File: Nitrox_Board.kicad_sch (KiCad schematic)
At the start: 9 parts

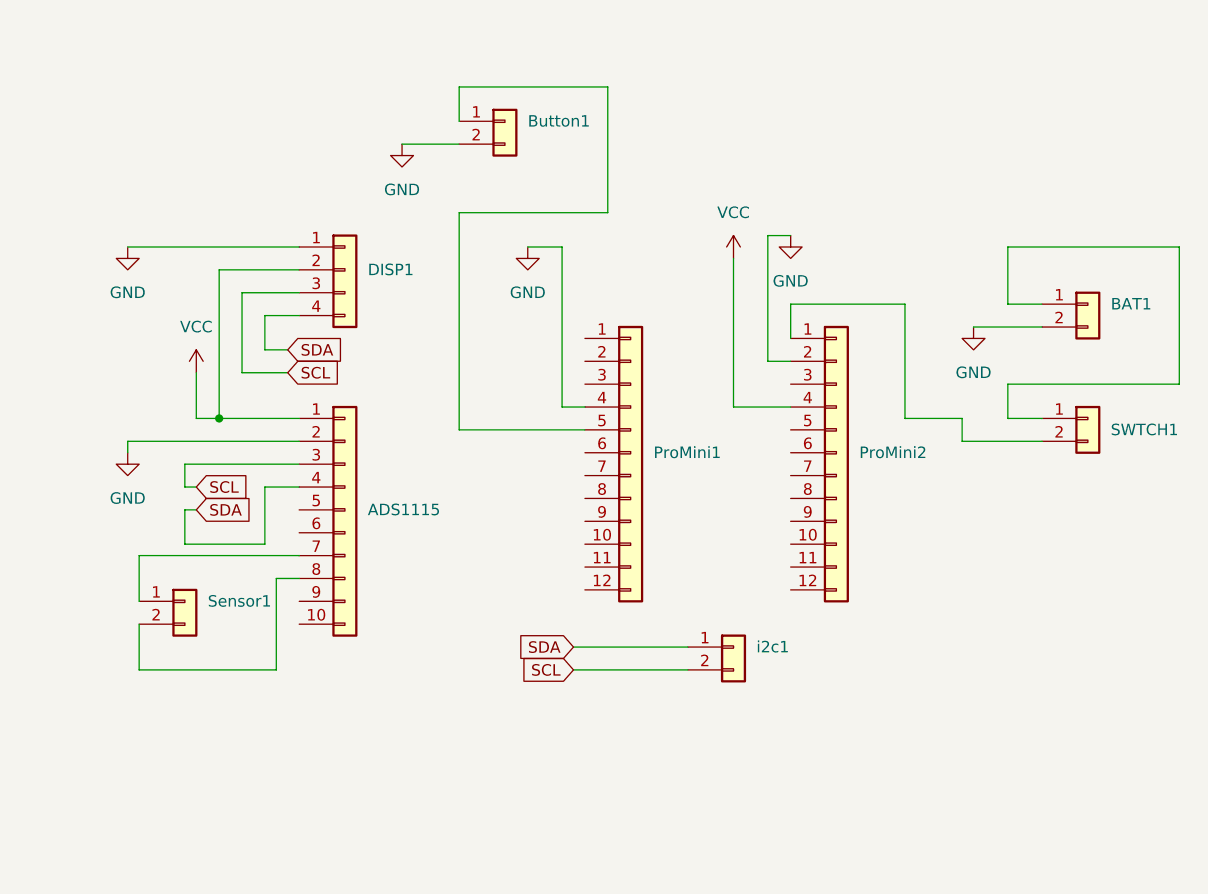
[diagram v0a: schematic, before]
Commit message: Initial Sketch
Pending some breadboard work, basic diagram and pinouts.
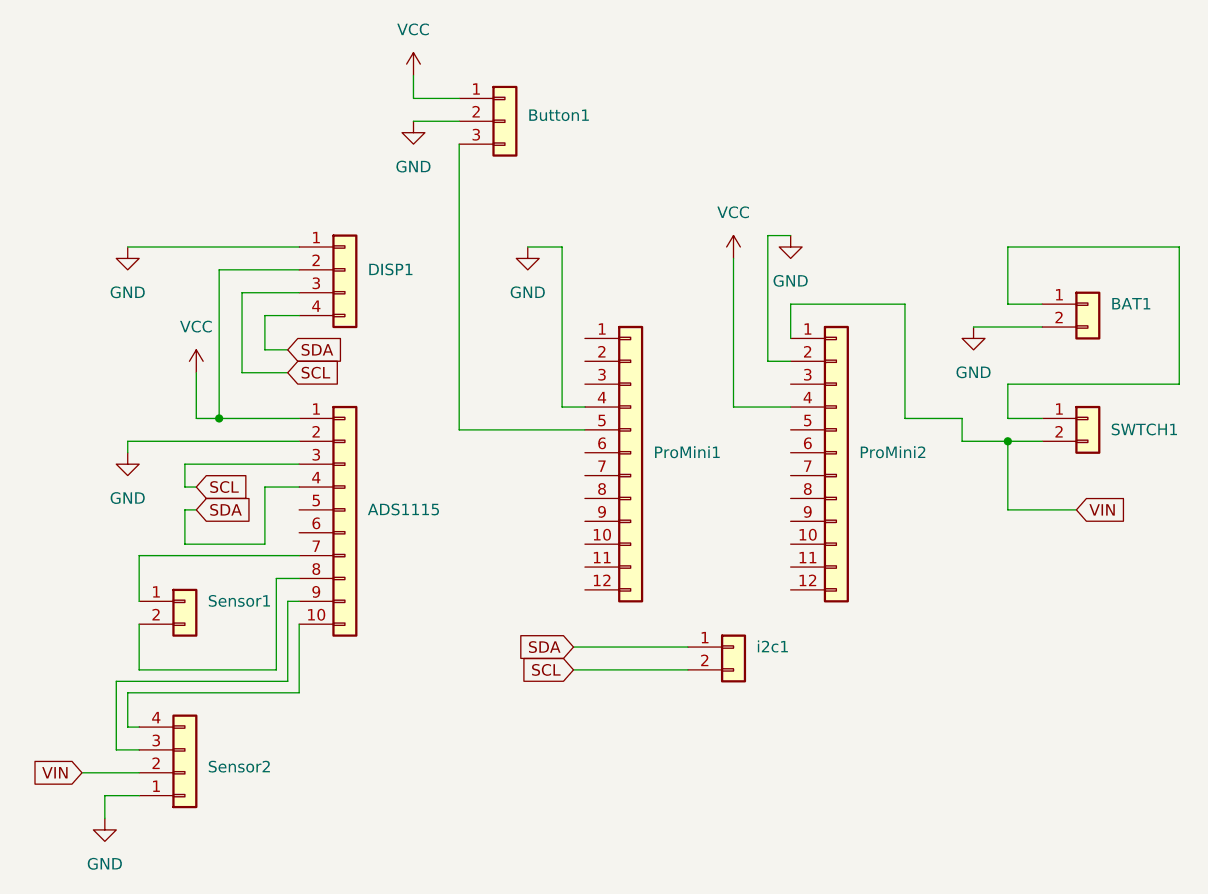
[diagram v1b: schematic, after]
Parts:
- added Sensor2: ~, Connector_JST:JST_XH_B2B-XH-A_1x02_P2.50mm_Vertical, symbol Connector_Generic:Conn_01x04
- Button1: symbol Connector_Generic:Conn_01x02 -> Connector_Generic:Conn_01x03
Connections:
- net GND: now also Sensor2.1 (Pin_1)
- net VCC: now also Button1.1 (Pin_1)
- net VIN: now reaches ProMini2.1 (Pin_1), SWTCH1.2 (Pin_2)
- net VIN: now also Sensor2.2 (Pin_2)
- net at ProMini1.5 (Pin_5): now also Button1.3 (Pin_3); no longer Button1.1 (Pin_1)
- net at ADS1115.10 (Pin_10): now also Sensor2.4 (Pin_4)
- net at ADS1115.9 (Pin_9): now also Sensor2.3 (Pin_3)

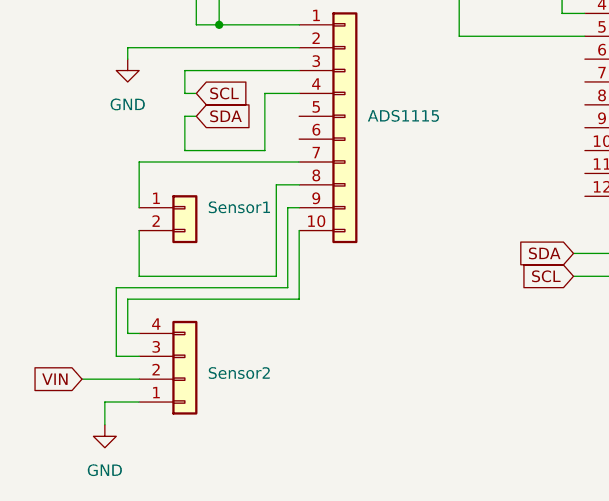
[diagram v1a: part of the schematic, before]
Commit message: CO Sensor Changes
Add CO Sensor Alarm to display render, add CO Sensor to ADC pin 3 (non-diff reading), Add various math/variables for CO Sensor and to differentiate from O2 Sensor, Always calibrate on Boot/Reset, and FREEDOM UNITS (MOD in Feet instead of meters).

PCB Updated to add CO Sensor leads and LED lead for button illumination when on.
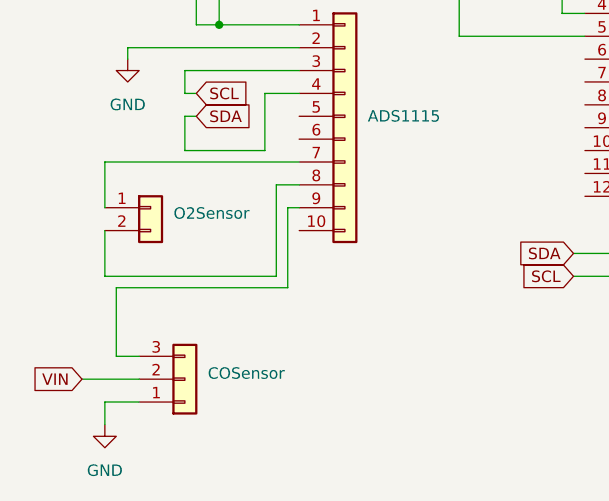
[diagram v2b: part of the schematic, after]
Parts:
- COSensor: renamed from Sensor2; symbol Connector_Generic:Conn_01x04 -> Connector_Generic:Conn_01x03
- renumbered Sensor1 to O2Sensor
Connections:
- net at ADS1115.10 (Pin_10): no longer COSensor.4 (Pin_4)
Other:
- moved on the sheet: O2Sensor
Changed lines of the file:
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@@
 	(wire
 		(pts
-			(xy 26.67 86.36) (xy 41.91 86.36)
-		)
-		(stroke
-			(width 0)
-			(type default)
-		)
-	)
-	(wire
-		(pts
-			(xy 26.67 73.66) (xy 44.45 73.66)
+			(xy 22.86 86.36) (xy 41.91 86.36)
+		)
+		(stroke
+			(width 0)
+			(type default)
+		)
+	)
+	(wire
+		(pts
+			(xy 22.86 73.66) (xy 44.45 73.66)
 		)
 		(stroke
@@
 	(wire
 		(pts
+			(xy 123.19 68.58) (xy 130.81 68.58)
+		)
+		(stroke
+			(width 0)
+			(type default)
+		)
+	)
+	(wire
+		(pts
+			(xy 40.64 72.39) (xy 31.75 72.39)
+		)
+		(stroke
+			(width 0)
+			(type default)
+		)
+	)
+	(wire
+		(pts
+			(xy 74.93 83.82) (xy 87.63 83.82)
+		)
+		(stroke
+			(width 0)
+			(type default)
+		)
+	)
+	(wire
+		(pts
+			(xy 119.38 48.26) (xy 127 48.26)
+		)
+		(stroke
+			(width 0)
+			(type default)
+		)
+	)
+	(wire
+		(pts
+			(xy 40.64 46.99) (xy 40.64 50.8)
+		)
+		(stroke
+			(width 0)
+			(type default)
+		)
+	)
+	(wire
+		(pts
+			(xy 92.71 57.15) (xy 99.06 57.15)
+		)
+		(stroke
+			(width 0)
+			(type default)
+		)
+	)
+	(wire
+		(pts
+			(xy 41.91 76.2) (xy 44.45 76.2)
+		)
+		(stroke
+			(width 0)
+			(type default)
+		)
+	)
+	(wire
+		(pts
+			(xy 22.86 81.28) (xy 22.86 86.36)
+		)
+		(stroke
+			(width 0)
+			(type default)
+		)
+	)
+	(wire
+		(pts
+			(xy 57.15 20.32) (xy 57.15 22.86)
+		)
+		(stroke
+			(width 0)
+			(type default)
+		)
+	)
+	(wire
+		(pts
+			(xy 123.19 60.96) (xy 123.19 68.58)
+		)
+		(stroke
+			(width 0)
+			(type default)
+		)
+	)
+	(wire
+		(pts
+			(xy 123.19 45.72) (xy 123.19 39.37)
+		)
+		(stroke
+			(width 0)
+			(type default)
+		)
+	)
+	(wire
+		(pts
+			(xy 127 45.72) (xy 123.19 45.72)
+		)
+		(stroke
+			(width 0)
+			(type default)
+		)
+	)
+	(wire
+		(pts
+			(xy 96.52 52.07) (xy 96.52 38.1)
+		)
+		(stroke
+			(width 0)
+			(type default)
+		)
+	)
+	(wire
+		(pts
+			(xy 38.1 53.34) (xy 43.18 53.34)
+		)
+		(stroke
+			(width 0)
+			(type default)
+		)
+	)
+	(wire
+		(pts
+			(xy 92.71 40.64) (xy 92.71 57.15)
+		)
+		(stroke
+			(width 0)
+			(type default)
+		)
+	)
+	(wire
+		(pts
+			(xy 123.19 54.61) (xy 123.19 58.42)
+		)
+		(stroke
+			(width 0)
+			(type default)
+		)
+	)
+	(wire
+		(pts
 			(xy 24.13 87.63) (xy 43.18 87.63)
 		)
@@
 	(wire
 		(pts
-			(xy 123.19 68.58) (xy 130.81 68.58)
-		)
-		(stroke
-			(width 0)
-			(type default)
-		)
-	)
-	(wire
-		(pts
-			(xy 40.64 72.39) (xy 31.75 72.39)
-		)
-		(stroke
-			(width 0)
-			(type default)
-		)
-	)
-	(wire
-		(pts
-			(xy 74.93 83.82) (xy 87.63 83.82)
-		)
-		(stroke
-			(width 0)
-			(type default)
-		)
-	)
-	(wire
-		(pts
-			(xy 25.4 88.9) (xy 25.4 92.71)
-		)
-		(stroke
-			(width 0)
-			(type default)
-		)
-	)
-	(wire
-		(pts
-			(xy 119.38 48.26) (xy 127 48.26)
-		)
-		(stroke
-			(width 0)
-			(type default)
-		)
-	)
-	(wire
-		(pts
-			(xy 25.4 88.9) (xy 44.45 88.9)
-		)
-		(stroke
-			(width 0)
-			(type default)
-		)
-	)
-	(wire
-		(pts
-			(xy 40.64 46.99) (xy 40.64 50.8)
-		)
-		(stroke
-			(width 0)
-			(type default)
-		)
-	)
-	(wire
-		(pts
-			(xy 92.71 57.15) (xy 99.06 57.15)
-		)
-		(stroke
-			(width 0)
-			(type default)
-		)
-	)
-	(wire
-		(pts
-			(xy 41.91 76.2) (xy 44.45 76.2)
-		)
-		(stroke
-			(width 0)
-			(type default)
-		)
-	)
-	(wire
-		(pts
-			(xy 26.67 81.28) (xy 26.67 86.36)
-		)
-		(stroke
-			(width 0)
-			(type default)
-		)
-	)
-	(wire
-		(pts
-			(xy 57.15 20.32) (xy 57.15 22.86)
-		)
-		(stroke
-			(width 0)
-			(type default)
-		)
-	)
-	(wire
-		(pts
-			(xy 123.19 60.96) (xy 123.19 68.58)
-		)
-		(stroke
-			(width 0)
-			(type default)
-		)
-	)
-	(wire
-		(pts
-			(xy 123.19 45.72) (xy 123.19 39.37)
-		)
-		(stroke
-			(width 0)
-			(type default)
-		)
-	)
-	(wire
-		(pts
-			(xy 127 45.72) (xy 123.19 45.72)
-		)
-		(stroke
-			(width 0)
-			(type default)
-		)
-	)
-	(wire
-		(pts
-			(xy 96.52 52.07) (xy 96.52 38.1)
-		)
-		(stroke
-			(width 0)
-			(type default)
-		)
-	)
-	(wire
-		(pts
-			(xy 38.1 53.34) (xy 43.18 53.34)
-		)
-		(stroke
-			(width 0)
-			(type default)
-		)
-	)
-	(wire
-		(pts
-			(xy 92.71 40.64) (xy 92.71 57.15)
-		)
-		(stroke
-			(width 0)
-			(type default)
-		)
-	)
-	(wire
-		(pts
-			(xy 123.19 54.61) (xy 123.19 58.42)
-		)
-		(stroke
-			(width 0)
-			(type default)
-		)
-	)
-	(wire
-		(pts
-			(xy 44.45 81.28) (xy 44.45 88.9)
-		)
-		(stroke
-			(width 0)
-			(type default)
-		)
-	)
-	(wire
-		(pts
 			(xy 40.64 50.8) (xy 43.18 50.8)
 		)
@@
 	(wire
 		(pts
-			(xy 26.67 92.71) (xy 25.4 92.71)
+			(xy 43.18 78.74) (xy 43.18 87.63)
 		)
 		(stroke
@@
 	(wire
 		(pts
-			(xy 43.18 87.63) (xy 43.18 78.74)
-		)
-		(stroke
-			(width 0)
-			(type default)
-		)
-	)
-	(wire
-		(pts
 			(xy 35.56 41.91) (xy 35.56 58.42)
 		)
@@
 	(wire
 		(pts
-			(xy 26.67 78.74) (xy 26.67 73.66)
+			(xy 22.86 78.74) (xy 22.86 73.66)
 		)
 		(stroke
@@
 	(symbol
 		(lib_id "Connector_Generic:Conn_01x02")
-		(at 31.75 78.74 0)
+		(at 27.94 78.74 0)
 		(unit 1)
 		(exclude_from_sim no)
@@
 		(dnp no)
 		(fields_autoplaced yes)
-		(property "Reference" "Sensor1"
-			(at 34.29 78.74 0)
+		(property "Reference" "O2Sensor"
+			(at 30.48 79.3749 0)
 			(effects
 				(font
@@
 		)
 		(property "Value" "~"
-			(at 34.29 81.28 0)
+			(at 30.48 81.28 0)
 			(effects
 				(font
@@
 		)
 		(property "Footprint" "Connector_JST:JST_XH_B2B-XH-A_1x02_P2.50mm_Vertical"
-			(at 31.75 78.74 0)
+			(at 27.94 78.74 0)
 			(effects
 				(font
@@
 		)
 		(property "Datasheet" "~"
-			(at 31.75 78.74 0)
+			(at 27.94 78.74 0)
 			(effects
 				(font
@@
 		)
 		(property "Description" ""
-			(at 31.75 78.74 0)
+			(at 27.94 78.74 0)
 			(effects
 				(font
@@
 			(project "Nitrox_Board"
 				(path "/f427a0c7-1886-4932-8356-bf0159ce0656"
-					(reference "Sensor1")
+					(reference "O2Sensor")
 					(unit 1)
 				)
@@
 	)
 	(symbol
-		(lib_id "Connector_Generic:Conn_01x04")
+		(lib_id "Connector_Generic:Conn_01x03")
 		(at 31.75 97.79 0)
 		(mirror x)
@@
 		(on_board yes)
 		(dnp no)
-		(property "Reference" "Sensor2"
+		(property "Reference" "COSensor"
 			(at 34.29 97.1551 0)
 			(effects
@@
 			)
 		)
-		(property "Description" "Generic connector, single row, 01x04, script generated (kicad-library-utils/schlib/autogen/connector/)"
+		(property "Description" "Generic connector, single row, 01x03, script generated (kicad-library-utils/schlib/autogen/connector/)"
 			(at 31.75 97.79 0)
 			(effects
@@
 		)
 		(pin "2"
-		)
-		(pin "4"
 		)
 		(pin "3"
@@
 			(project "Nitrox_Board"
 				(path "/f427a0c7-1886-4932-8356-bf0159ce0656"
-					(reference "Sensor2")
+					(reference "COSensor")
 					(unit 1)
 				)
